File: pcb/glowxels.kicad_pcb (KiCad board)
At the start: 2 copper layers, 79 parts, among them J1 OUT, J2 IN, U1 STP16CPC26, U2 STP16CPC26, U3 STP16CPC26, U4 STP16CPC26

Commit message: First version, fully routed.
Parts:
- added C10: 47u, Capacitor_SMD:C_1210_3225Metric, F.Cu at (73.3, 49.1)
- added C11: 47u, Capacitor_SMD:C_1210_3225Metric, F.Cu at (60.5, 44.1)
- added C12: 47u, Capacitor_SMD:C_1210_3225Metric, F.Cu at (60.5, 49.1)
- added C6: 47u, Capacitor_SMD:C_1210_3225Metric, F.Cu at (98.6, 44.1)
- added C7: 47u, Capacitor_SMD:C_1210_3225Metric, F.Cu at (86.2, 49.1)
- added C8: 47u, Capacitor_SMD:C_1210_3225Metric, F.Cu at (86.2, 44.1)
- added C9: 47u, Capacitor_SMD:C_1210_3225Metric, F.Cu at (73.3, 44.1)
- C5: value 100u -> 47u; footprint Capacitor_SMD:CP_Elec_6.3x5.3 -> Capacitor_SMD:C_1210_3225Metric
- J1: value OUT -> Conn_01x06_Pin; footprint Glowxels:EdgeConnect -> Connector_PinHeader_2.00mm:PinHeader_1x06_P2.00mm_Vertical
- J2: value IN -> Conn_01x02_Pin; footprint Glowxels:EdgeConnect -> Connector_PinHeader_2.00mm:PinHeader_1x02_P2.00mm_Vertical
- moved J2 73.2 mm to (51.3, 40.6), turned to -90 degrees
- moved J1 59.7 mm to (101.2, 40.6), turned to -90 degrees
- moved R1 56.8 mm to (49.2, 48.5), turned to 90 degrees
- moved C1 53.9 mm to (49.2, 45.4), turned to -90 degrees
- moved R2 50.2 mm to (64.4, 41.3), turned to -90 degrees
- moved C2 44.8 mm to (62.9, 41.3), turned to 90 degrees
- moved R3 44.3 mm to (77.2, 41.3), turned to -90 degrees
- moved R4 42.1 mm to (89.0, 41.3), turned to -90 degrees
- moved C3 37.0 mm to (75.7, 41.3), turned to 90 degrees
- moved C4 33.7 mm to (86.3, 41.0), turned to 180 degrees
- moved C5 20.6 mm to (98.6, 49.1), turned to -90 degrees
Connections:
- J1 pad 1: /VDD -> GND
- J1 pad 2: /D-Out -> /Latch
- J1 pad 3: /~{OE} -> /CLK
- J1 pad 4: /CLK -> /D-IN
- J1 pad 5: /Latch -> /VDD
- J2 pad 1: /VDD -> GND
- J2 pad 2: /D-IN -> /LED-Power
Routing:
- net /LED-Power: track 0.00 -> 92.4 mm, vias 0 -> 8
- net /Latch: track 0.00 -> 72.7 mm, vias 0 -> 4
- net /CLK: track 0.00 -> 69.6 mm, vias 0 -> 4
- net /VDD: track 0.00 -> 58.1 mm, vias 0 -> 4
- net /~{OE}: track 0.00 -> 52.9 mm, vias 0 -> 3
- net Net-(U3-SDI): track 0.00 -> 17.5 mm
- net Net-(U1-SDI): track 0.00 -> 17.5 mm
- net Net-(U2-SDI): track 0.00 -> 17.5 mm
- net /D-IN: track 0.00 -> 15.9 mm
- net Net-(D9-K): track 0.00 -> 7.12 mm, vias 0 -> 1
- net Net-(D41-K): track 0.00 -> 7.12 mm, vias 0 -> 1
- net Net-(D25-K): track 0.00 -> 7.12 mm, vias 0 -> 1
- net Net-(D8-K): track 0.00 -> 6.12 mm, vias 0 -> 1
- net Net-(D24-K): track 0.00 -> 6.12 mm, vias 0 -> 1
- net Net-(D40-K): track 0.00 -> 6.12 mm, vias 0 -> 1
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- added copper zone on B.Cu, net /LED-Power
- added copper zone on B.Cu, net GND
- added copper zone on F.Cu, net GND
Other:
- board outline added: 55.2 x 14 mm
- board text added: "CLK"
- board text added: "DIN"
- board text added: "GND"
- board text added: "LAT"
- board text added: "VCC"
- board text added: "VLED"
- board text added: "~{OE}"

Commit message: Update with Labels.
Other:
- board text added: "%%gitversion%%"
- board text added: "Tiny Glowxels | https://github.com/hzeller/glowxels"
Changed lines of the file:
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@@
+		)
+	)
+	(gr_text "%%gitversion%%"
+		(at 100.9 41.8 270)
+		(layer "F.SilkS")
+		(effects
+			(font
+				(size 0.6 0.6)
+				(thickness 0.1)
+				(bold yes)
+			)
+			(justify left bottom)
 		)
 	)
@@
 		)
 	)
+	(gr_text "Tiny Glowxels | https://github.com/hzeller/glowxels"
+		(at 73.3 52.6 0)
+		(layer "F.SilkS")
+		(effects
+			(font
+				(size 0.6 0.6)
+				(thickness 0.1)
+				(bold yes)
+			)
+			(justify bottom)
+		)
+	)

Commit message: Some more GND layer stiching.
The kind of fiddling with the design after it has been sent to
fab already :)
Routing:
- net /Latch: track 72.7 -> 73.4 mm
- net /CLK: track 69.6 -> 70.1 mm
- net GND: vias 21 -> 27
- added copper zone on F.Cu, net /LED-Power
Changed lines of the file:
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@@
 		(tags "capacitor")
 		(property "Reference" "C4"
-			(at 2.6 0.1 360)
+			(at 2.6 0.1 0)
 			(layer "F.SilkS")
 			(effects
@@
 		)
 		(property "Value" "100n"
-			(at 0 1.43 360)
+			(at 0 1.43 0)
 			(layer "F.Fab")
 			(effects
@@
 		)
 		(fp_text user "${REFERENCE}"
-			(at 0 0 360)
+			(at 0 0 0)
 			(layer "F.Fab")
 			(effects
@@
 		(tags "LED")
 		(property "Reference" "D2"
-			(at -4.5 0.1 270)
+			(at -4.5 0.1 -90)
 			(layer "B.SilkS")
 			(hide yes)
@@
 		(tags "LED")
 		(property "Reference" "D51"
-			(at -4.5 0.1 270)
+			(at -4.5 0.1 -90)
 			(layer "B.SilkS")
 			(hide yes)
@@
 		(tags "LED")
 		(property "Reference" "D1"
-			(at -4.5 0.1 270)
+			(at -4.5 0.1 -90)
 			(layer "B.SilkS")
 			(hide yes)
@@
 		(tags "LED")
 		(property "Reference" "D56"
-			(at -4.5 0.1 270)
+			(at -4.5 0.1 -90)
 			(layer "B.SilkS")
 			(hide yes)
@@
 		(tags "LED")
 		(property "Reference" "D53"
-			(at -4.5 0.1 270)
+			(at -4.5 0.1 -90)
 			(layer "B.SilkS")
 			(hide yes)
@@
 		(tags "LED")
 		(property "Reference" "D52"
-			(at -4.5 0.1 270)
+			(at -4.5 0.1 -90)
 			(layer "B.SilkS")
 			(hide yes)
@@
 		(tags "LED")
 		(property "Reference" "D55"
-			(at -4.5 0.1 270)
+			(at -4.5 0.1 -90)
 			(layer "B.SilkS")
 			(hide yes)
@@
 		(tags "LED")
 		(property "Reference" "D54"
-			(at -4.5 0.1 270)
+			(at -4.5 0.1 -90)
 			(layer "B.SilkS")
 			(hide yes)
@@
 		(tags "LED")
 		(property "Reference" "D50"
-			(at -4.5 0.1 270)
+			(at -4.5 0.1 -90)
 			(layer "B.SilkS")
 			(hide yes)
@@
 	)
 	(via
+		(at 75 43)
+		(size 0.635)
+		(drill 0.254)
+		(layers "F.Cu" "B.Cu")
+		(free yes)
+		(net 2)
+	)
+	(via
+		(at 100.75 45)
+		(size 0.635)
+		(drill 0.254)
+		(layers "F.Cu" "B.Cu")
+		(free yes)
+		(net 2)
+	)
+	(via
 		(at 74 52.9)
 		(size 0.635)
@@
 	)
 	(via
+		(at 87.5 43.25)
+		(size 0.635)
+		(drill 0.254)
+		(layers "F.Cu" "B.Cu")
+		(free yes)
+		(net 2)
+	)
+	(via
 		(at 88.4 50.6)
 		(size 0.635)
@@
 	)
 	(via
+		(at 101.25 48.25)
+		(size 0.635)
+		(drill 0.254)
+		(layers "F.Cu" "B.Cu")
+		(free yes)
+		(net 2)
+	)
+	(via
+		(at 62.25 43)
+		(size 0.635)
+		(drill 0.254)
+		(layers "F.Cu" "B.Cu")
+		(free yes)
+		(net 2)
+	)
+	(via
 		(at 61.2 39.8)
 		(size 0.635)
@@
 	)
 	(via
-		(at 102.4 49.8)
+		(at 102.4 50.5)
 		(size 0.635)
 		(drill 0.254)
@@
 	)
 	(via
-		(at 87.1 39.8)
+		(at 71.5 45)
 		(size 0.635)
 		(drill 0.254)
@@
 	)
 	(via
-		(at 59.7 39.8)
+		(at 87.1 39.8)
 		(size 0.635)
 		(drill 0.254)
@@
 	)
 	(via
-		(at 102.4 43.4)
+		(at 59.7 39.8)
 		(size 0.635)
 		(drill 0.254)
@@
 	)
 	(via
-		(at 102.4 46.6)
+		(at 102.4 42.75)
 		(size 0.635)
 		(drill 0.254)
@@
 	)
 	(via
+		(at 57.25 45)
+		(size 0.635)
+		(drill 0.254)
+		(layers "F.Cu" "B.Cu")
+		(free yes)
+		(net 2)
+	)
+	(via
 		(at 61.1 52.9)
 		(size 0.635)
@@
 	)
 	(segment
+		(start 98.871617 52.237499)
+		(end 102.25 48.859116)
+		(width 0.2)
+		(layer "B.Cu")
+		(net 68)
+	)
+	(segment
 		(start 76.8925 52.2075)
 		(end 77.5 51.6)
@@
 	)
 	(segment
-		(start 101.495 42.895)
-		(end 101.495 49.614117)
-		(width 0.2)
-		(layer "B.Cu")
-		(net 68)
-	)
-	(segment
 		(start 90.8375 52.2375)
 		(end 90.2 51.6)
@@
 	)
 	(segment
+		(start 99.2 41.016709)
+		(end 99.2 40.6)
+		(width 0.2)
+		(layer "B.Cu")
+		(net 68)
+	)
+	(segment
 		(start 63.9925 52.3075)
 		(end 64.7 51.6)
@@
 	)
 	(segment
-		(start 101.495 49.614117)
-		(end 98.871617 52.2375)
+		(start 102.25 48.859116)
+		(end 102.25 44.066709)
+		(width 0.2)
+		(layer "B.Cu")
+		(net 68)
+	)
+	(segment
+		(start 98.871617 52.2375)
+		(end 98.871617 52.237499)
 		(width 0.2)
 		(layer "B.Cu")
@@
 	)
 	(segment
-		(start 99.2 40.6)
-		(end 101.495 42.895)
+		(start 102.25 44.066709)
+		(end 99.2 41.016709)
 		(width 0.2)
 		(layer "B.Cu")
@@
 	)
 	(segment
-		(start 101.135 49.465)
-		(end 98.7225 51.8775)
-		(width 0.2)
-		(layer "B.Cu")
-		(net 69)
-	)
-	(segment
 		(start 76.1325 51.8675)
 		(end 66.02375 51.8675)
@@
 	(segment
 		(start 98.7225 51.8775)
-		(end 91.5775 51.8775)
-		(width 0.2)
-		(layer "B.Cu")
-		(net 69)
-	)
-	(segment
-		(start 101.135 44.535)
-		(end 101.135 49.465)
+		(end 101.8275 48.7725)
 		(width 0.2)
 		(layer "B.Cu")
@@
 	)
 	(segment
-		(start 97.2 40.6)
-		(end 101.135 44.535)
-		(width 0.2)
-		(layer "B.Cu")
-		(net 69)
-	)
-	(segment
 		(start 66.02375 51.8675)
 		(end 64.65625 50.5)
@@
 	)
 	(segment
-		(start 91.5775 51.8775)
-		(end 90.2 50.5)
+		(start 101.8275 48.7725)
+		(end 101.8275 45.2275)
 		(width 0.2)
 		(layer "B.Cu")
@@
 	)
 	(segment
+		(start 90.2 50.5)
+		(end 91.5775 51.8775)
+		(width 0.2)
+		(layer "B.Cu")
+		(net 69)
+	)
+	(segment
 		(start 77.5 50.5)
 		(end 76.1325 51.8675)
@@
 	)
 	(segment
+		(start 91.5775 51.8775)
+		(end 98.7225 51.8775)
+		(width 0.2)
+		(layer "B.Cu")
+		(net 69)
+	)
+	(segment
 		(start 78.8675 51.8675)
 		(end 77.5 50.5)
@@
 	)
 	(segment
+		(start 101.8275 45.2275)
+		(end 97.2 40.6)
+		(width 0.2)
+		(layer "B.Cu")
+		(net 69)
+	)
+	(segment
 		(start 91.025 40.975)
 		(end 91.5 40.5)
@@
 	)
 	(zone
+		(net 3)
+		(net_name "/LED-Power")
+		(layer "F.Cu")
+		(hatch edge 0.5)
+		(priority 2)
+		(connect_pads
+			(clearance 0.18)
+		)
+		(min_thickness 0.25)
+		(filled_areas_thickness no)
+		(fill yes
+			(thermal_gap 0.5)
+			(thermal_bridge_width 0.5)
+		)
+		(polygon
+			(pts
+				(xy 87.5 46.25) (xy 87.5 47) (xy 84.75 47) (xy 84.75 46.25)
+			)
+		)
+	)
+	(zone
+		(net 3)
+		(net_name "/LED-Power")
+		(layer "F.Cu")
+		(hatch edge 0.5)
+		(priority 2)
+		(connect_pads
+			(clearance 0.18)
+		)
+		(min_thickness 0.25)
+		(filled_areas_thickness no)
+		(fill yes
+			(thermal_gap 0.5)
+			(thermal_bridge_width 0.5)
+		)
+		(polygon
+			(pts
+				(xy 59.25 46.25) (xy 61.75 46.25) (xy 61.75 47) (xy 59.25 47)
+			)
+		)
+	)
+	(zone
 		(net 2)
 		(net_name "GND")
@@
 			)
 		)
+	)
+	(zone
+		(net 3)
+		(net_name "/LED-Power")
+		(layer "F.Cu")
+		(hatch edge 0.5)
+		(priority 2)
+		(connect_pads
+			(clearance 0.18)
+		)
+		(min_thickness 0.25)
+		(filled_areas_thickness no)
+		(fill yes
+			(thermal_gap 0.5)
+			(thermal_bridge_width 0.5)
+		)
+		(polygon
+			(pts
+				(xy 72 46.25) (xy 74.5 46.25) (xy 74.5 47) (xy 72 47)
+			)
+		)
+	)
+	(zone
+		(net 3)
+		(net_name "/LED-Power")
+		(layer "F.Cu")
+		(hatch edge 0.5)
+		(priority 2)
+		(connect_pads
+			(clearance 0.18)
+		)
+		(min_thickness 0.25)
+		(filled_areas_thickness no)
+		(fill yes
+			(thermal_gap 0.5)
+			(thermal_bridge_width 0.5)
+		)
+		(polygon
+			(pts
+				(xy 97.25 46.25) (xy 100 46.25) (xy 100 47) (xy 97.25 47)
+			)
+		)

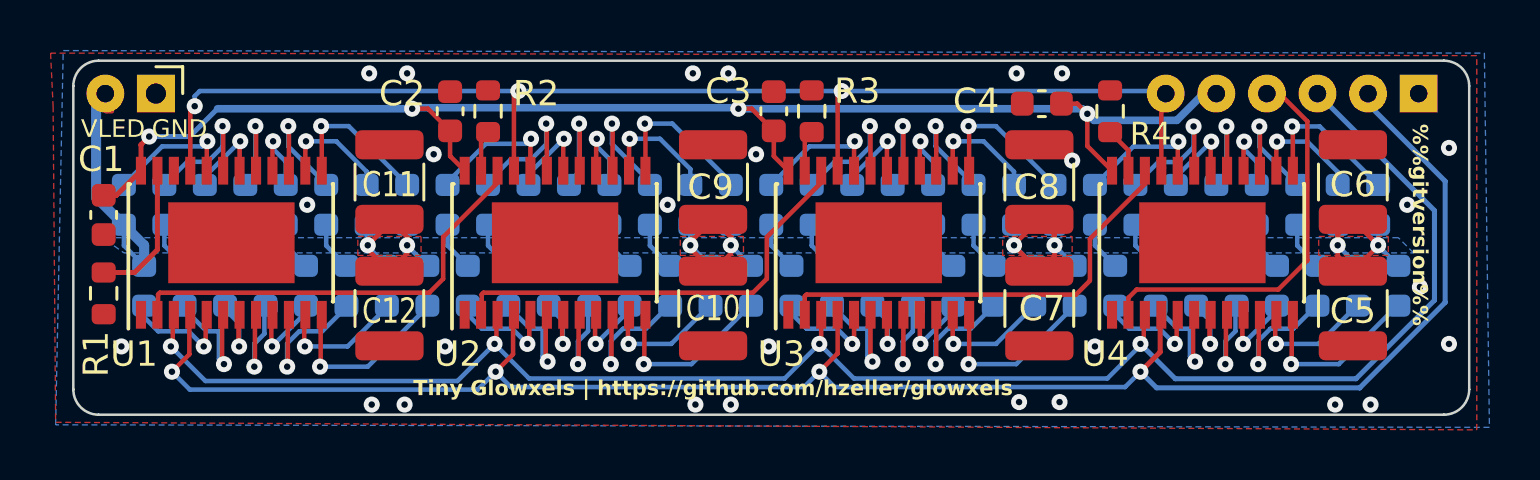
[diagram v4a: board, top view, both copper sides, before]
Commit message: Make fillet tracks.
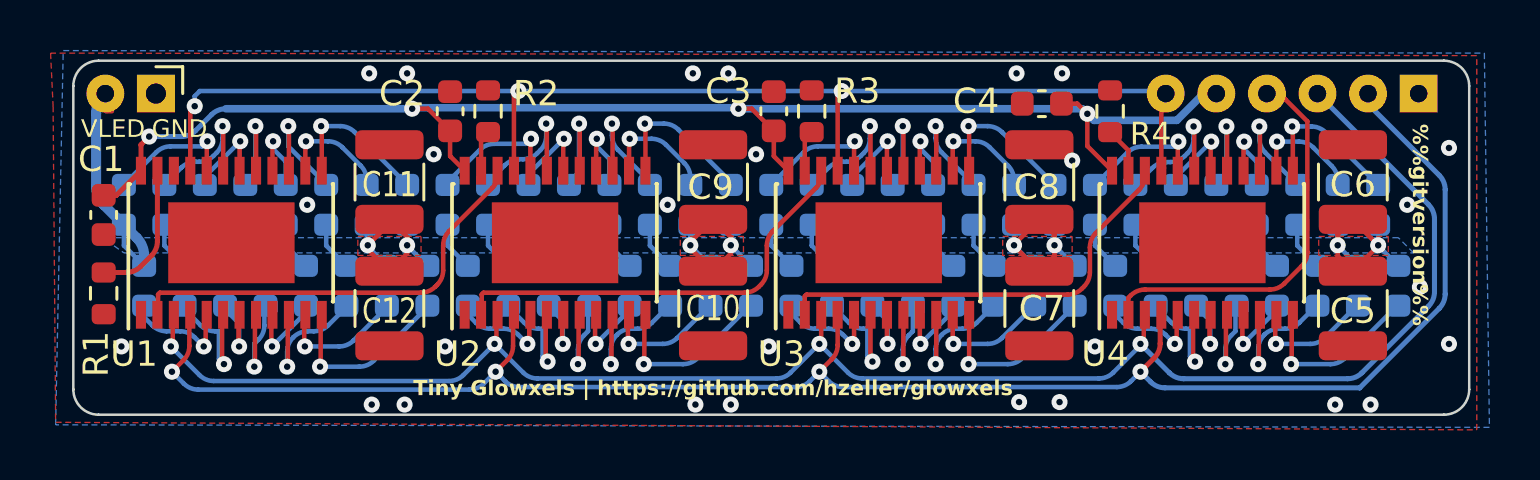
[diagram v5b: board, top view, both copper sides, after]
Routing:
- net /D-IN: track 15.9 -> 16.6 mm
- net /Latch: track 73.4 -> 72.8 mm
